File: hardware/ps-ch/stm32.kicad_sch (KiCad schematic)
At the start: 15 parts, among them J1 Conn_02x05_Odd_Even, U12 STM32C031K4Tx

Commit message: did some wiring
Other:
- note added: "STM32"
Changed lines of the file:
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@@
+		)
+	)
+	(text "STM32"
+		(exclude_from_sim no)
+		(at 143.256 31.75 0)
+		(effects
+			(font
+				(size 6.35 6.35)
+				(thickness 1.27)
+				(bold yes)
+			)
 		)
 	)

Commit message: drawn enabled circuit
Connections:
- net ~{OCP}: now reaches U12.1 (PB9)
- net DISCHARGE_OUTPUT: now reaches U12.17 (PB2)
- no-connect marks 10 -> 8
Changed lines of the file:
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@@
-	)
-	(no_connect
-		(at 133.35 86.36)
 	)
 	(no_connect
@@
 	)
 	(no_connect
-		(at 133.35 104.14)
-	)
-	(no_connect
 		(at 153.67 71.12)
 	)
@@
 	(wire
 		(pts
+			(xy 115.57 104.14) (xy 133.35 104.14)
+		)
+		(stroke
+			(width 0)
+			(type default)
+		)
+	)
+	(wire
+		(pts
 			(xy 153.67 88.9) (xy 158.75 88.9)
 		)
@@
 		(pts
 			(xy 173.99 53.34) (xy 173.99 55.88)
+		)
+		(stroke
+			(width 0)
+			(type default)
+		)
+	)
+	(wire
+		(pts
+			(xy 115.57 86.36) (xy 133.35 86.36)
 		)
 		(stroke
@@
 		)
 	)
+	(hierarchical_label "DISCHARGE_OUTPUT"
+		(shape output)
+		(at 115.57 86.36 180)
+		(effects
+			(font
+				(size 1.27 1.27)
+			)
+			(justify right)
+		)
+	)
 	(hierarchical_label "STM32_SPI_MISO"
 		(shape input)
@@
 		)
 	)
+	(hierarchical_label "~{OCP}"
+		(shape input)
+		(at 115.57 104.14 180)
+		(effects
+			(font
+				(size 1.27 1.27)
+			)
+			(justify right)
+		)
+	)

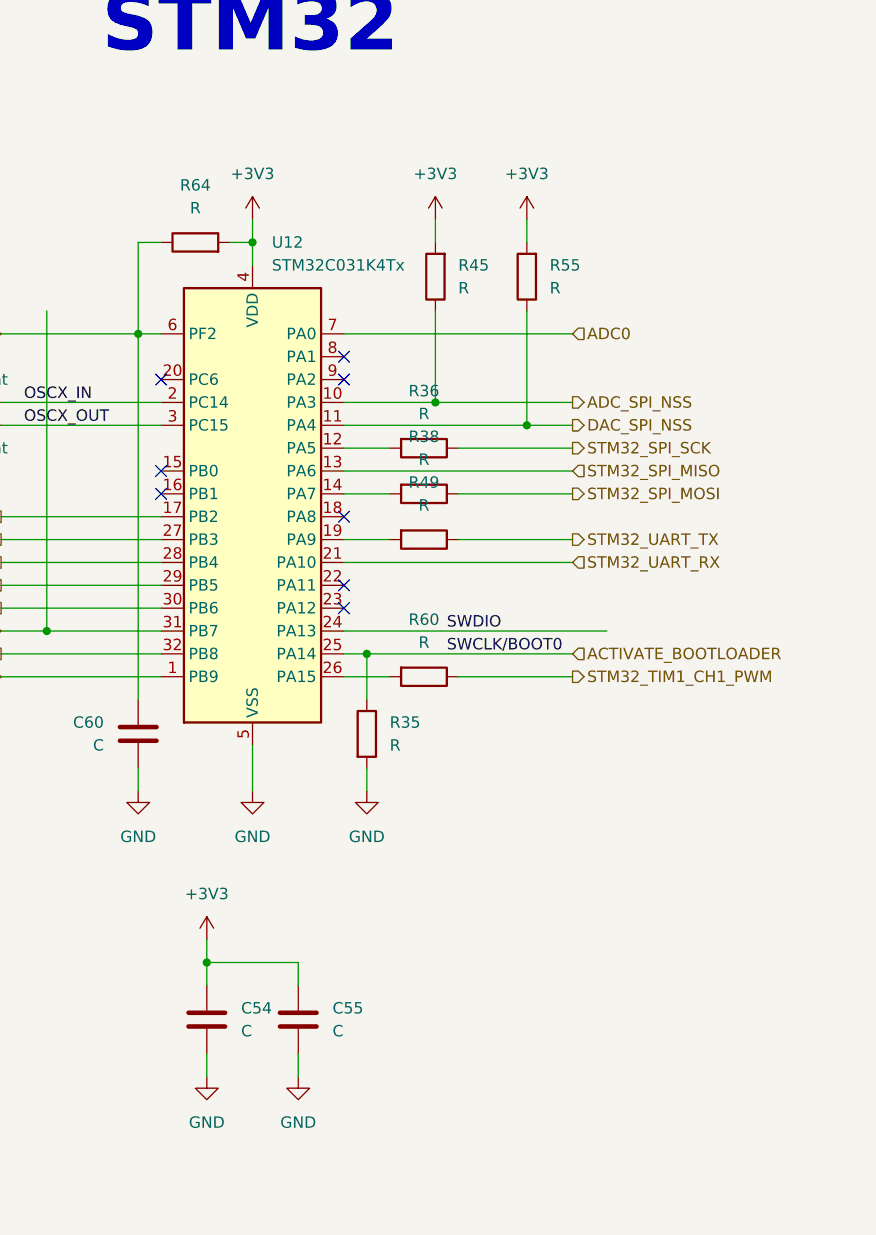
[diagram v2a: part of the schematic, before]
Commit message: - added component values/part numbers
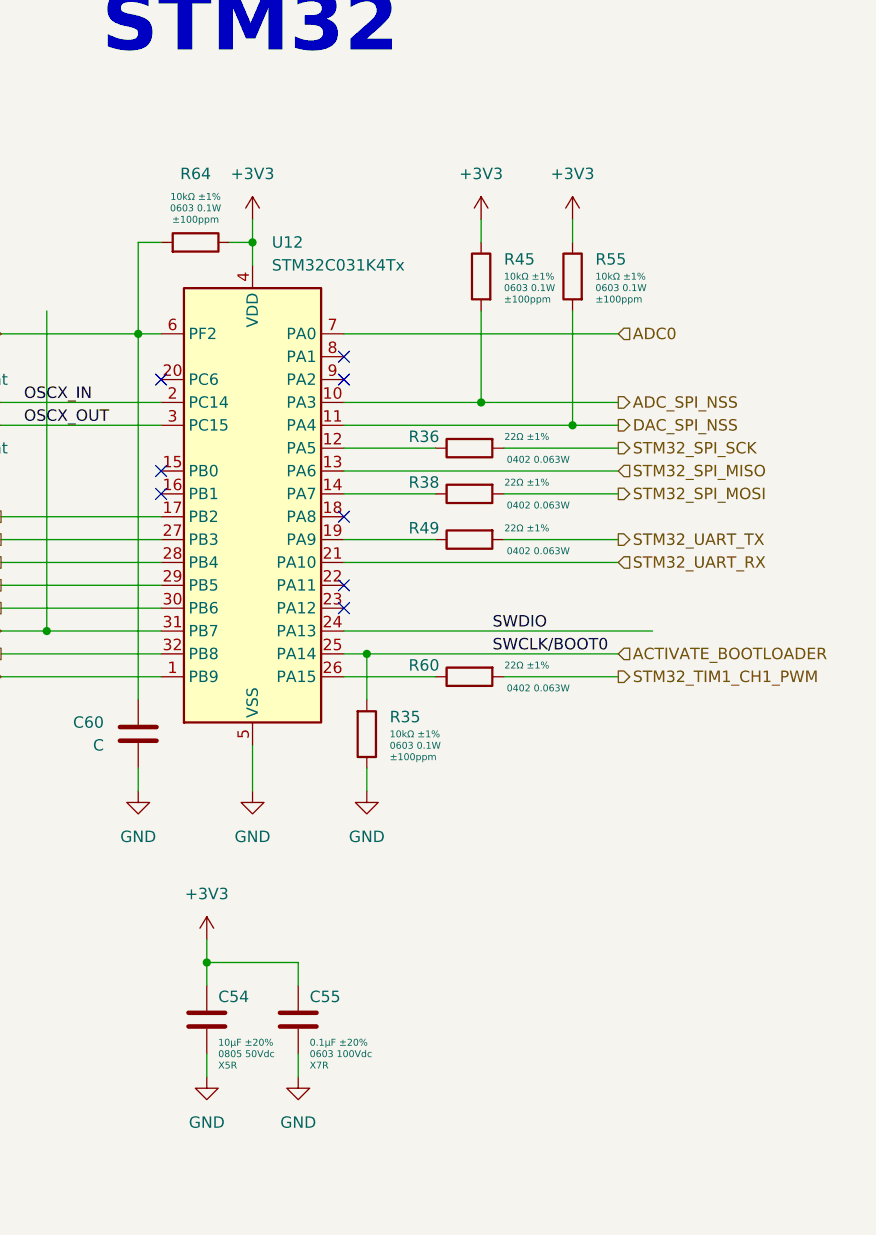
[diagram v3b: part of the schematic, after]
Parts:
- C54: value C -> 10μF 0805 50Vdc X5R ±20%; footprint (none) -> Capacitor_SMD:C_0805_2012Metric; symbol Device:C -> ps-ch:10μF 0805 50Vdc X5R ±20%; DisplayValue0 (none) -> 10μF ±20%; DisplayValue1 (none) -> 0805 50Vdc; DisplayValue2 (none) -> X5R; Manufacturer (none) -> Murata; Manufacturer Part Number (none) -> GRM21BR61H106ME43
- C55: value C -> 0.1μF 0603 100Vdc X7R ±20%; footprint (none) -> Capacitor_SMD:C_0603_1608Metric; symbol Device:C -> ps-ch:0.1μF 0603 100Vdc X7R ±20%; DisplayValue0 (none) -> 0.1μF ±20%; DisplayValue1 (none) -> 0603 100Vdc; DisplayValue2 (none) -> X7R; Manufacturer (none) -> Murata; Manufacturer Part Number (none) -> GRM188R72A104MA35
- R35, R45, R55, R64: value R -> 10kΩ 0603 0.1W ±1% ±100ppm/°C; footprint (none) -> Resistor_SMD:R_0603_1608Metric; symbol Device:R -> ps-ch:10kΩ 0603 0.1W ±1% ±100ppm/°C; DisplayValue0 (none) -> 10kΩ ±1%; DisplayValue1 (none) -> 0603 0.1W; DisplayValue2 (none) -> ±100ppm; Manufacturer (none) -> Yageo; Manufacturer Part Number (none) -> AC0603FR-071K2L
- R36, R38, R49, R60: value R -> 22Ω 0402 0.063W ±1% ±100ppm/°C; footprint (none) -> Resistor_SMD:R_0402_1005Metric; symbol Device:R -> ps-ch:22Ω 0402 0.063W ±1% ±100ppm/°C; DisplayValue0 (none) -> 22Ω ±1%; DisplayValue1 (none) -> 0402 0.063W; DisplayValue2 (none) -> ±100ppm; Manufacturer (none) -> Yageo; Manufacturer Part Number (none) -> AC0402FR-0722RL
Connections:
- net +3V3: now also C54.2, C55.2, R45.1, R55.1, R64.1; no longer C54.1, C55.1, R45.2, R55.2, R64.2
- net ACTIVATE_BOOTLOADER: now also R35.2; no longer R35.1
- net ADC_SPI_NSS: now also R45.2; no longer R45.1
- net DAC_SPI_NSS: now also R55.2; no longer R55.1
- net GND: now also C54.1, C55.1, R35.1; no longer C54.2, C55.2, R35.2
- net STM32_SPI_MOSI: now also R38.2; no longer R38.1
- net STM32_SPI_SCK: now also R36.2; no longer R36.1
- net STM32_TIM1_CH1_PWM: now also R60.2; no longer R60.1
- net STM32_UART_TX: now also R49.2; no longer R49.1
- net ~{STM32_RST}: now also R64.2; no longer R64.1
- net at U12.12 (PA5): now also R36.1; no longer R36.2
- net at U12.19 (PA9): now also R49.1; no longer R49.2
- net at U12.14 (PA7): now also R38.1; no longer R38.2
- net at U12.26 (PA15): now also R60.1; no longer R60.2
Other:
- moved on the sheet: R36, R38, R45, R49, R55, R60

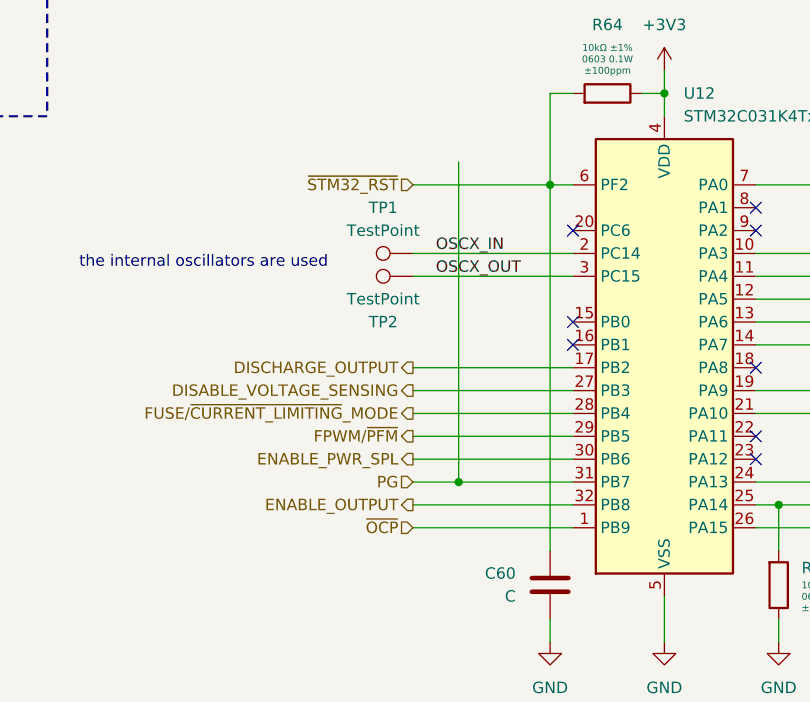
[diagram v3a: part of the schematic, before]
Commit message: added calculations and component values
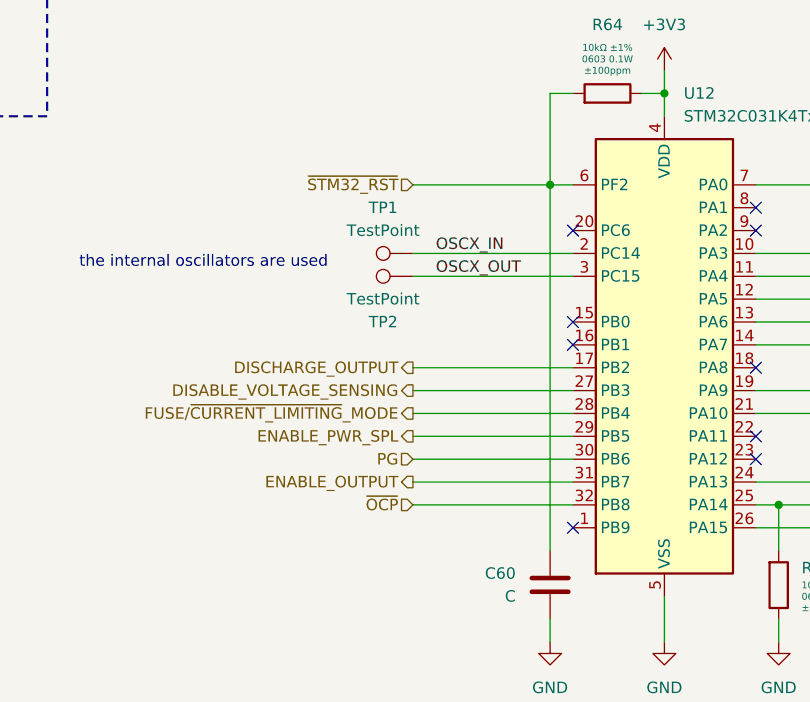
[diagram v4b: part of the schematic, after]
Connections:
- net FPWM/~{PFM} is gone; now on net ENABLE_PWR_SPL: U12.29 (PB5)
- net ENABLE_OUTPUT: now also U12.31 (PB7); no longer U12.32 (PB8)
- net ENABLE_PWR_SPL: no longer U12.30 (PB6)
- net PG: now also U12.30 (PB6); no longer U12.31 (PB7)
- net ~{OCP}: now also U12.32 (PB8); no longer U12.1 (PB9)
- no-connect marks 8 -> 9
